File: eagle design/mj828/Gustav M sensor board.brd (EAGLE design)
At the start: 20 x 40 mm, 10 parts, among them IC1 AH1913-W-7, IC2 AH1913-W-7

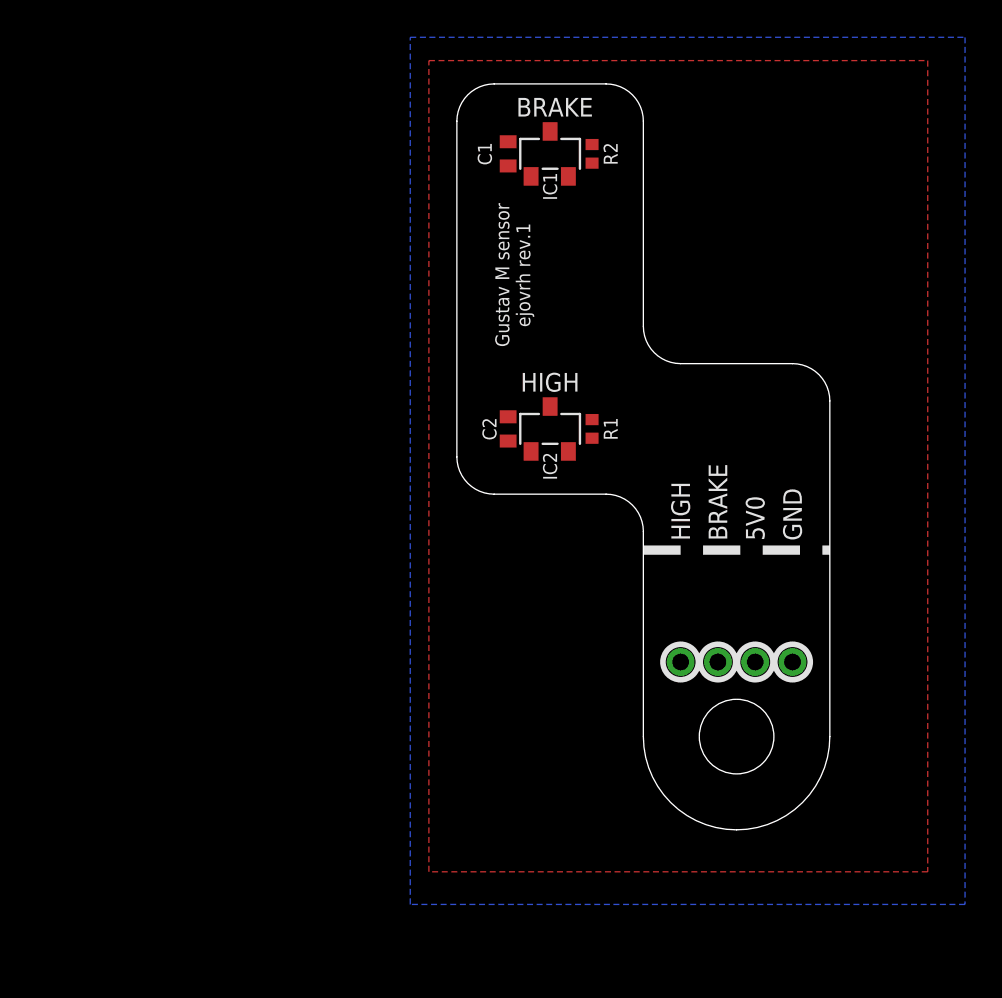
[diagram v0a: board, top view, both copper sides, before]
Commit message: - preliminary gustav m sensor board routed
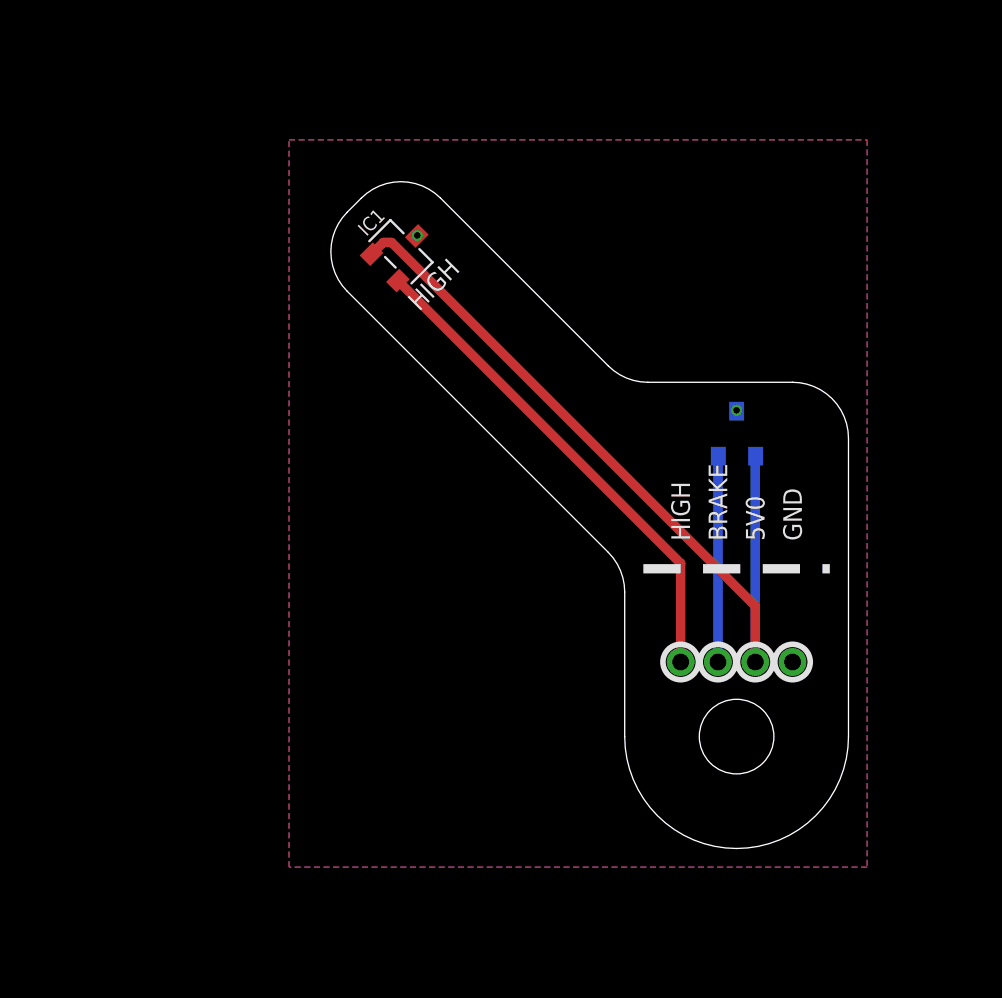
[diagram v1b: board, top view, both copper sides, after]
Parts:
- removed C1, C2: 0.1μF, rcl:C0402
- removed R1, R2: 10k, rcl:R0402
- moved IC2 10.0 mm to (15.0, 21.2), flipped to the bottom
- moved IC1 9.57 mm to (-3.00, 31.0), turned to 315 degrees
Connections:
- net 5V0: no longer C1.1, C2.2
- net BRAKE: now also IC2.2_OUT; no longer IC1.2_OUT, R2.1
- net GND: no longer C1.2, C2.1, R1.2, R2.2
- net HIGH: now also IC1.2_OUT; no longer IC2.2_OUT, R1.1
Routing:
- net 5V0: track 0.00 -> 43.0 mm
- net HIGH: track 0.00 -> 26.7 mm
- net BRAKE: track 0.00 -> 11.0 mm
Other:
- board size 20 x 40 mm -> 27.8 x 35.8 mm

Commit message: - gustav m sensor board progress
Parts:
- moved IC1 4.47 mm to (1.00, 33.0), turned to 300 degrees
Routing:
- net 5V0: track 43.0 -> 45.0 mm
- net HIGH: track 26.7 -> 25.8 mm
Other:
- board size 27.8 x 35.8 mm -> 23.1 x 37.5 mm

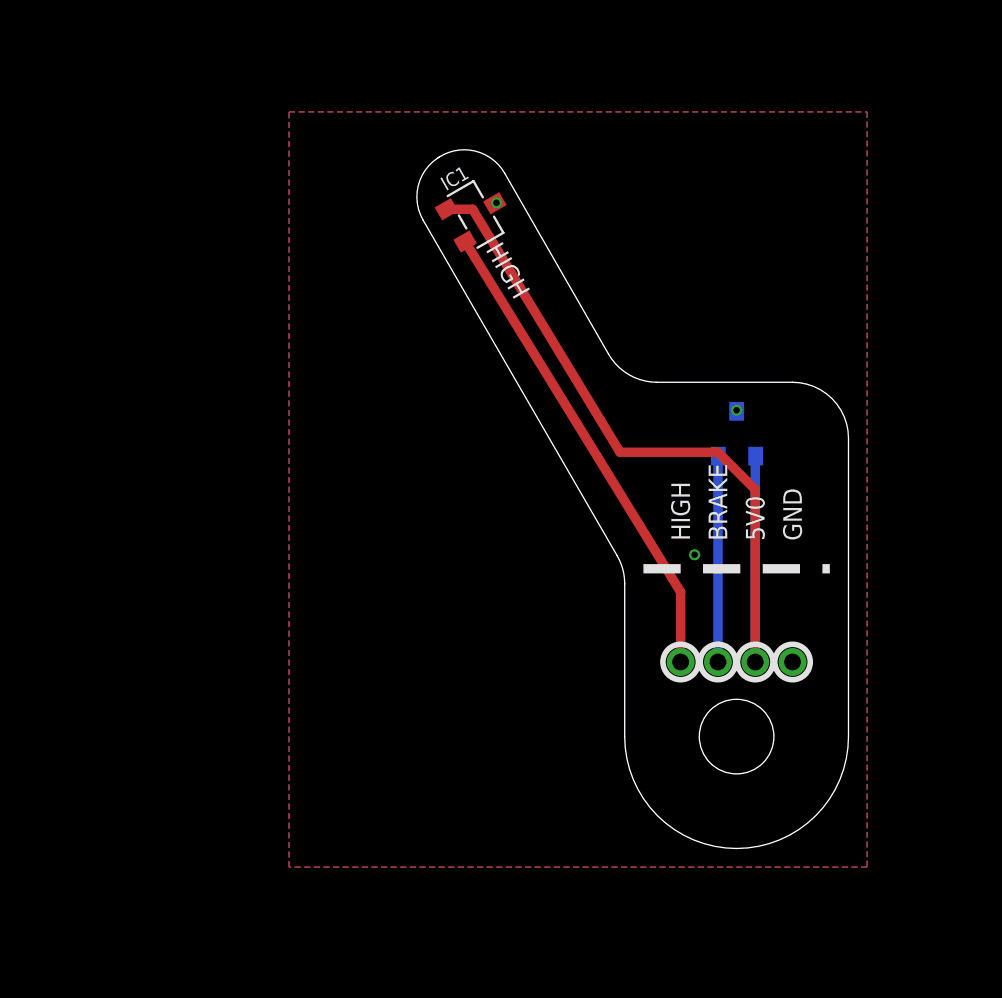
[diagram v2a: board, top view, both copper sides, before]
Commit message: Gustav M sensor board HW rev. 1 finished, submitted for production
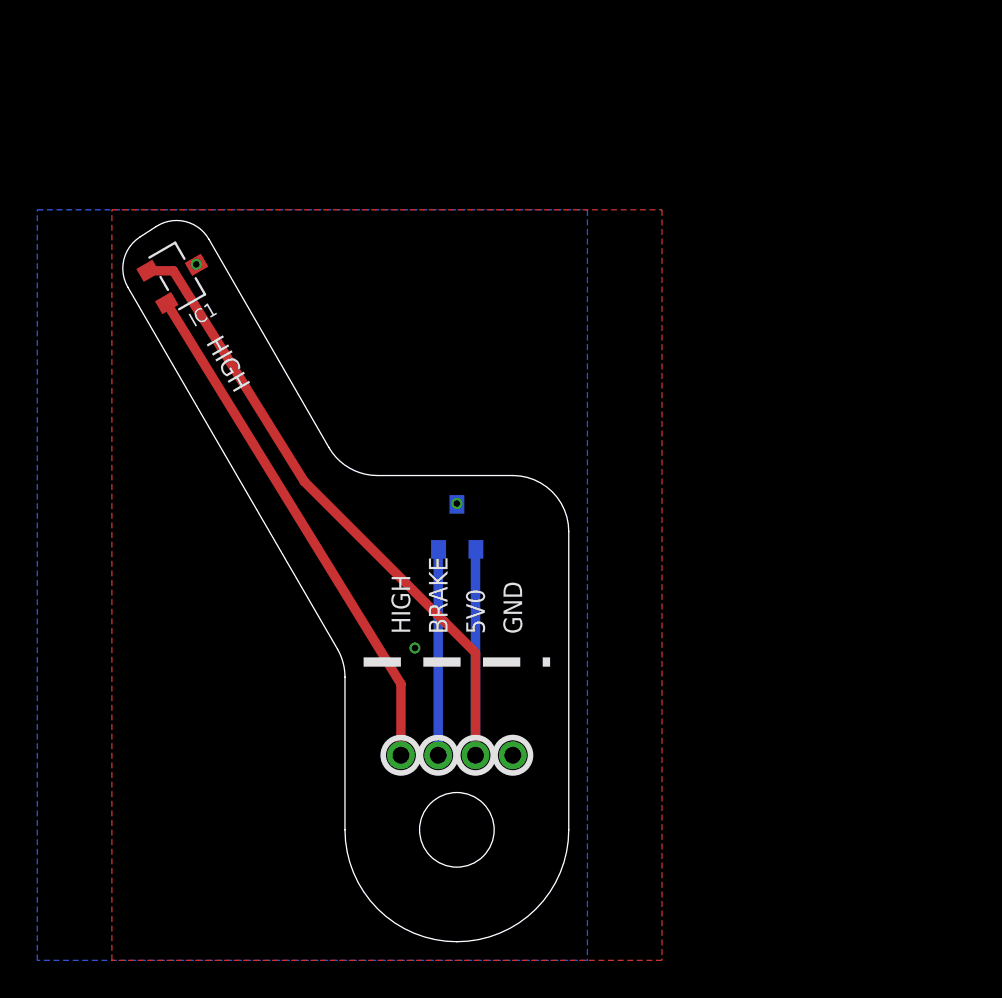
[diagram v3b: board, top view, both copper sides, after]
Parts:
- moved IC1 16.3 mm to (-15.0, 29.7)
- moved 5V0 15.8 mm to (1.00, 4.00)
- moved BRAKE 15.8 mm to (-1.00, 4.00)
- moved GND 15.8 mm to (3.00, 4.00)
- moved HIGH 15.8 mm to (-3.00, 4.00)
- moved IC2 15.8 mm to (0.00, 16.2)
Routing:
- net HIGH: track 25.8 -> 27.8 mm
- net 5V0: track 45.0 -> 44.2 mm
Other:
- board size 23.1 x 37.5 mm -> 23.9 x 38.7 mm
